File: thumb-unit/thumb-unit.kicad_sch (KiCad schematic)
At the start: 0 parts

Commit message: feat: oyayubi unit
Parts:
- added BT1: Battery, symbol Device:Battery
- added C10: 10uF, symbol Device:C
- added C11, C12: 10nF, symbol Device:C
- added C13, C15, C16: 100nF, symbol Device:C
- added C17: 3.3uF, symbol Device:C
- added D1, D2, D3, D4: D, symbol Device:D
- added J1: Conn_01x10, symbol Connector_Generic:Conn_01x10
- added R2: 10k, symbol Device:R
- added SW1: SW_SPDT, symbol Switch:SW_SPDT
- added SW2, SW3, SW4, SW5: SW_Push, symbol Switch:SW_Push
- added U1: xiao-ble, symbol mcu:xiao-ble
- added U2: PMW3610, sensor:PMW3610, symbol sensor:PMW3610
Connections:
- new net: D3.1 (K), SW4.1
- new net: D4.1 (K), SW5.1
- new net: D2.1 (K), SW3.1
- new net: C13.1, U2.13 (C-)
- new net: C13.2, U2.12 (C+)
- new net: BT1.1 (+), SW1.2 (B)
- new net: D1.1 (K), SW2.1
- new net: C10.1, C11.1, U2.9 (VCP)
- new net +3V3: C12.1, C12.2, C15.2, C16.2, C17.2, J1.1 (Pin_1), R2.1, U1.12 (3V3), U2.1 (+VCSEL), U2.14 (VDD), U2.15 (XYLASER), U2.16 (-VCSEL), U2.6 (VDDIO), U2.7 (~{RESET})
- new net BAT_SW: SW1.1 (A), U1.19 (BAT)
- new net COL0: J1.6 (Pin_6), SW2.2, U1.8 (B9_RX/1.12)
- new net COL1: J1.7 (Pin_7), SW3.2, U1.9 (A7_SCK/1.13)
- new net COL2: J1.8 (Pin_8), SW4.2, U1.10 (A5_MISO/1.14)
- new net COL3: J1.9 (Pin_9), SW5.2, U1.11 (A6_MOSI/1.15)
- new net COL4: J1.10 (Pin_10), U1.22 (NFC2/0.10_H)
- new net GND: BT1.2 (-), C10.2, C11.2, C15.1, C16.1, C17.1, J1.2 (Pin_2), U1.13 (GND), U1.18 (GND), U1.20 (GND), U2.11 (GND)
- new net MOTION: R2.2, U1.3 (A10/0.28), U2.8 (MOTION)
- new net NCS: U1.21 (NFC1/0.09_H), U2.5 (~{CS})
- new net ROW0: J1.3 (Pin_3), U1.4 (A11/0.29)
- new net ROW1: J1.4 (Pin_4), U1.5 (A8_SDA/0.04_H)
- new net ROW2: J1.5 (Pin_5), U1.6 (A9_SCL/0.05_H)
- new net ROW3: D1.2 (A), D2.2 (A), D3.2 (A), D4.2 (A), U1.7 (B8_TX/1.11)
- new net SCLK: U1.2 (A4/0.03_H), U2.3 (SCLK)
- new net SDIO: U1.1 (A2/0.02_H), U2.2 (SDIO)
- no-connect marks 0 -> 6

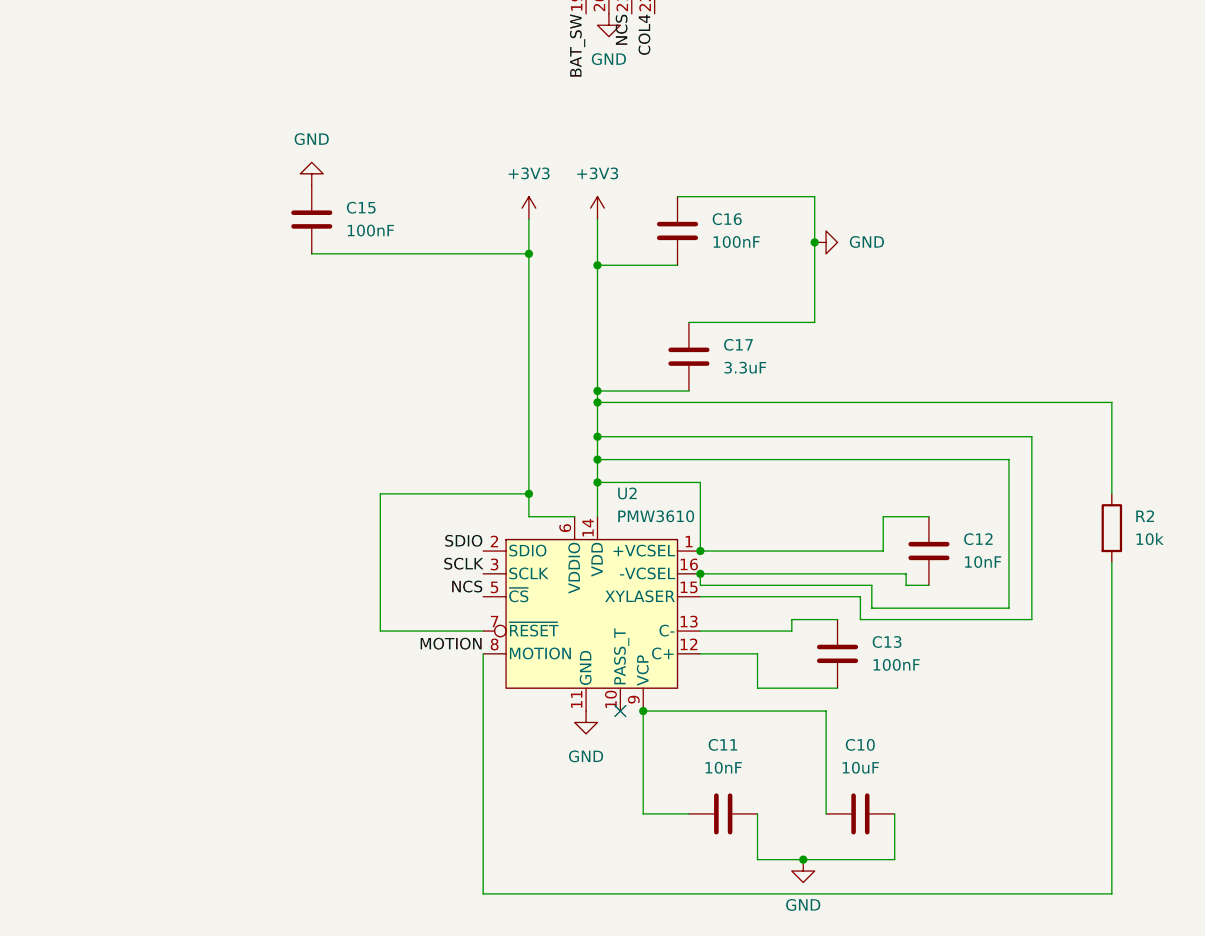
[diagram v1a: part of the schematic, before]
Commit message: feat: add ldo
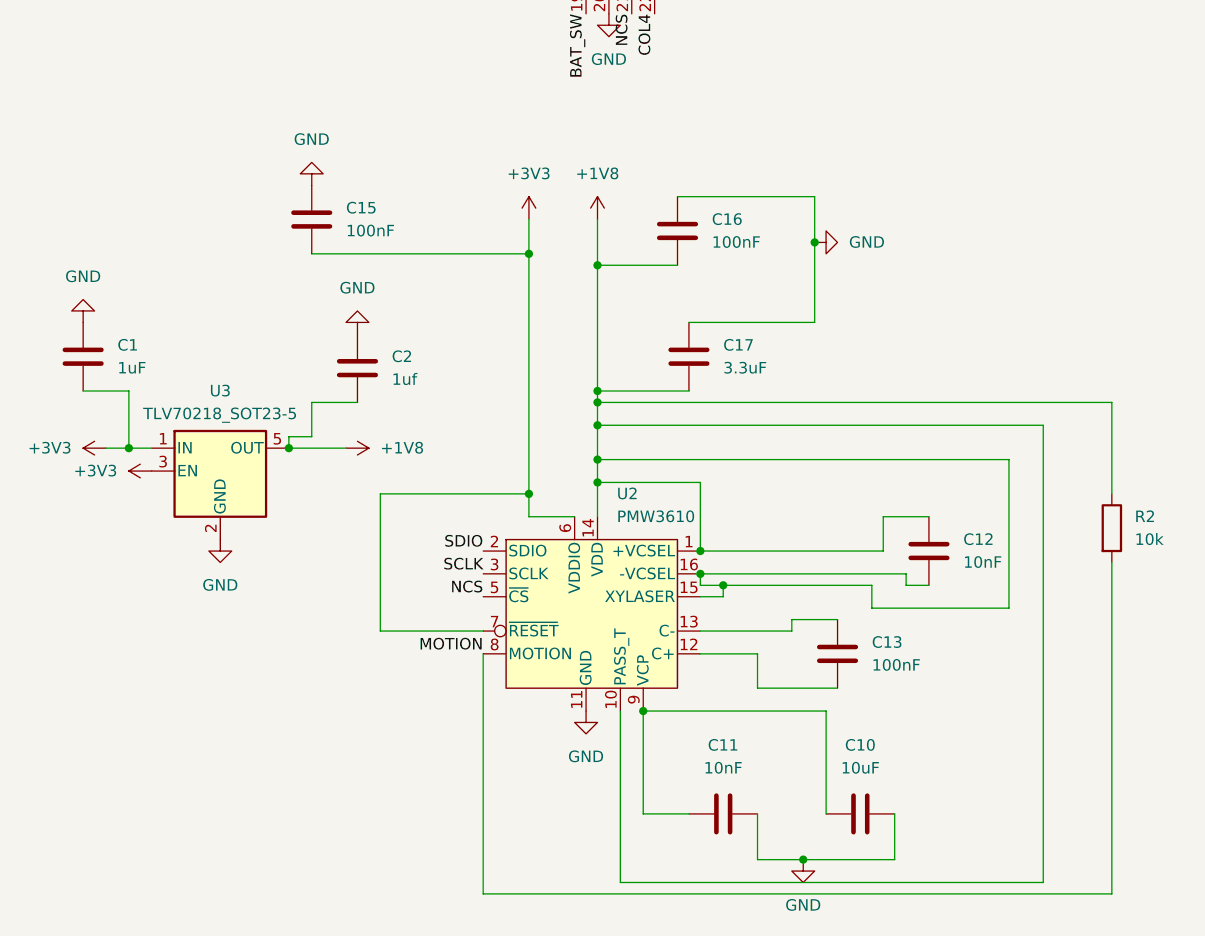
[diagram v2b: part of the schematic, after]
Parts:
- added C1: 1uF, symbol Device:C
- added C2: 1uf, symbol Device:C
- added U3: TLV70218_SOT23-5, Package_TO_SOT_SMD:SOT-23-5, symbol Regulator_Linear:TLV70218_SOT23-5
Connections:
- net +3V3: now also C1.2, U3.1 (IN), U3.3 (EN); no longer C12.1, C12.2, C16.2, C17.2, R2.1, U2.1 (+VCSEL), U2.14 (VDD), U2.15 (XYLASER), U2.16 (-VCSEL)
- net GND: now also C1.1, C2.1, U3.2 (GND)
- net +1V8: now reaches U2.10 (PASS_T)
- net +1V8: now also C12.1, C12.2, C16.2, C17.2, R2.1, U2.1 (+VCSEL), U2.14 (VDD), U2.15 (XYLASER), U2.16 (-VCSEL), C2.2, U3.5 (OUT)
- no-connect marks 6 -> 5

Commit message: feat: フットプリント割り当て
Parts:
- BT1: footprint (none) -> Connector_JST:JST_PH_S2B-PH-K_1x02_P2.00mm_Horizontal
- C1, C11, C12, C13, C15, C16, C17, C2: footprint (none) -> Capacitor_SMD:C_0402_1005Metric
- C10: footprint (none) -> Capacitor_SMD:C_0603_1608Metric
- D1, D2, D3, D4: footprint (none) -> Diode_SMD:D_SOD-123
- J1: footprint (none) -> Connector_FFC-FPC:Hirose_FH12-10S-0.5SH_1x10-1MP_P0.50mm_Horizontal
- R2: footprint (none) -> Resistor_SMD:R_0402_1005Metric
- SW1: footprint (none) -> custom:TGSW_MSK-12D19
- SW2, SW3, SW4, SW5: footprint (none) -> PCM_Switch_Keyboard_Hotswap_Kailh:SW_Hotswap_Kailh_Choc_V1V2_1.00u
- U1: footprint (none) -> mcu:xiao-ble-smd
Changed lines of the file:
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@@
 			)
 		)
-		(property "Footprint" ""
+		(property "Footprint" "Diode_SMD:D_SOD-123"
 			(at 190.5 114.3 0)
 			(effects
@@
 			)
 		)
-		(property "Footprint" ""
+		(property "Footprint" "Resistor_SMD:R_0402_1005Metric"
 			(at 131.572 149.86 90)
 			(effects
@@
 			)
 		)
-		(property "Footprint" ""
+		(property "Footprint" "Diode_SMD:D_SOD-123"
 			(at 204.47 114.3 0)
 			(effects
@@
 			)
 		)
-		(property "Footprint" ""
+		(property "Footprint" "Connector_FFC-FPC:Hirose_FH12-10S-0.5SH_1x10-1MP_P0.50mm_Horizontal"
 			(at 246.38 125.73 0)
 			(effects
@@
 			)
 		)
-		(property "Footprint" ""
+		(property "Footprint" "Diode_SMD:D_SOD-123"
 			(at 176.53 114.3 0)
 			(effects
@@
 			)
 		)
-		(property "Footprint" ""
+		(property "Footprint" "Capacitor_SMD:C_0402_1005Metric"
 			(at 103.8352 167.64 0)
 			(effects
@@
 			)
 		)
-		(property "Footprint" ""
+		(property "Footprint" "Capacitor_SMD:C_0402_1005Metric"
 			(at 20.0152 134.62 0)
 			(effects
@@
 			)
 		)
-		(property "Footprint" ""
+		(property "Footprint" "Connector_JST:JST_PH_S2B-PH-K_1x02_P2.00mm_Horizontal"
 			(at 161.29 157.226 90)
 			(effects
@@
 			)
 		)
-		(property "Footprint" ""
+		(property "Footprint" "Capacitor_SMD:C_0402_1005Metric"
 			(at 50.4952 135.89 0)
 			(effects
@@
 			)
 		)
-		(property "Footprint" ""
+		(property "Footprint" "mcu:xiao-ble-smd"
 			(at 73.66 71.12 0)
 			(effects
@@
 			)
 		)
-		(property "Footprint" ""
+		(property "Footprint" "PCM_Switch_Keyboard_Hotswap_Kailh:SW_Hotswap_Kailh_Choc_V1V2_1.00u"
 			(at 176.53 124.46 0)
 			(effects
@@
 			)
 		)
-		(property "Footprint" ""
+		(property "Footprint" "Capacitor_SMD:C_0402_1005Metric"
 			(at 113.9952 156.21 0)
 			(effects
@@
 			)
 		)
-		(property "Footprint" ""
+		(property "Footprint" "Capacitor_SMD:C_0402_1005Metric"
 			(at 86.0552 120.65 0)
 			(effects
@@
 			)
 		)
-		(property "Footprint" ""
+		(property "Footprint" "Diode_SMD:D_SOD-123"
 			(at 162.56 114.3 0)
 			(effects
@@
 			)
 		)
-		(property "Footprint" ""
+		(property "Footprint" "Capacitor_SMD:C_0402_1005Metric"
 			(at 87.3252 134.62 0)
 			(effects
@@
 			)
 		)
-		(property "Footprint" ""
+		(property "Footprint" "PCM_Switch_Keyboard_Hotswap_Kailh:SW_Hotswap_Kailh_Choc_V1V2_1.00u"
 			(at 204.47 124.46 0)
 			(effects
@@
 			)
 		)
-		(property "Footprint" ""
+		(property "Footprint" "Capacitor_SMD:C_0402_1005Metric"
 			(at 45.4152 119.38 0)
 			(effects
@@
 			)
 		)
-		(property "Footprint" ""
+		(property "Footprint" "Capacitor_SMD:C_0402_1005Metric"
 			(at 93.98 180.6448 0)
 			(effects
@@
 			)
 		)
-		(property "Footprint" ""
+		(property "Footprint" "Capacitor_SMD:C_0603_1608Metric"
 			(at 109.22 180.6448 0)
 			(effects
@@
 			)
 		)
-		(property "Footprint" ""
+		(property "Footprint" "PCM_Switch_Keyboard_Hotswap_Kailh:SW_Hotswap_Kailh_Choc_V1V2_1.00u"
 			(at 162.56 124.46 0)
 			(effects
@@
 			)
 		)
-		(property "Footprint" ""
+		(property "Footprint" "custom:TGSW_MSK-12D19"
 			(at 184.15 158.75 0)
 			(effects
@@
 			)
 		)
-		(property "Footprint" ""
+		(property "Footprint" "PCM_Switch_Keyboard_Hotswap_Kailh:SW_Hotswap_Kailh_Choc_V1V2_1.00u"
 			(at 190.5 124.46 0)
 			(effects

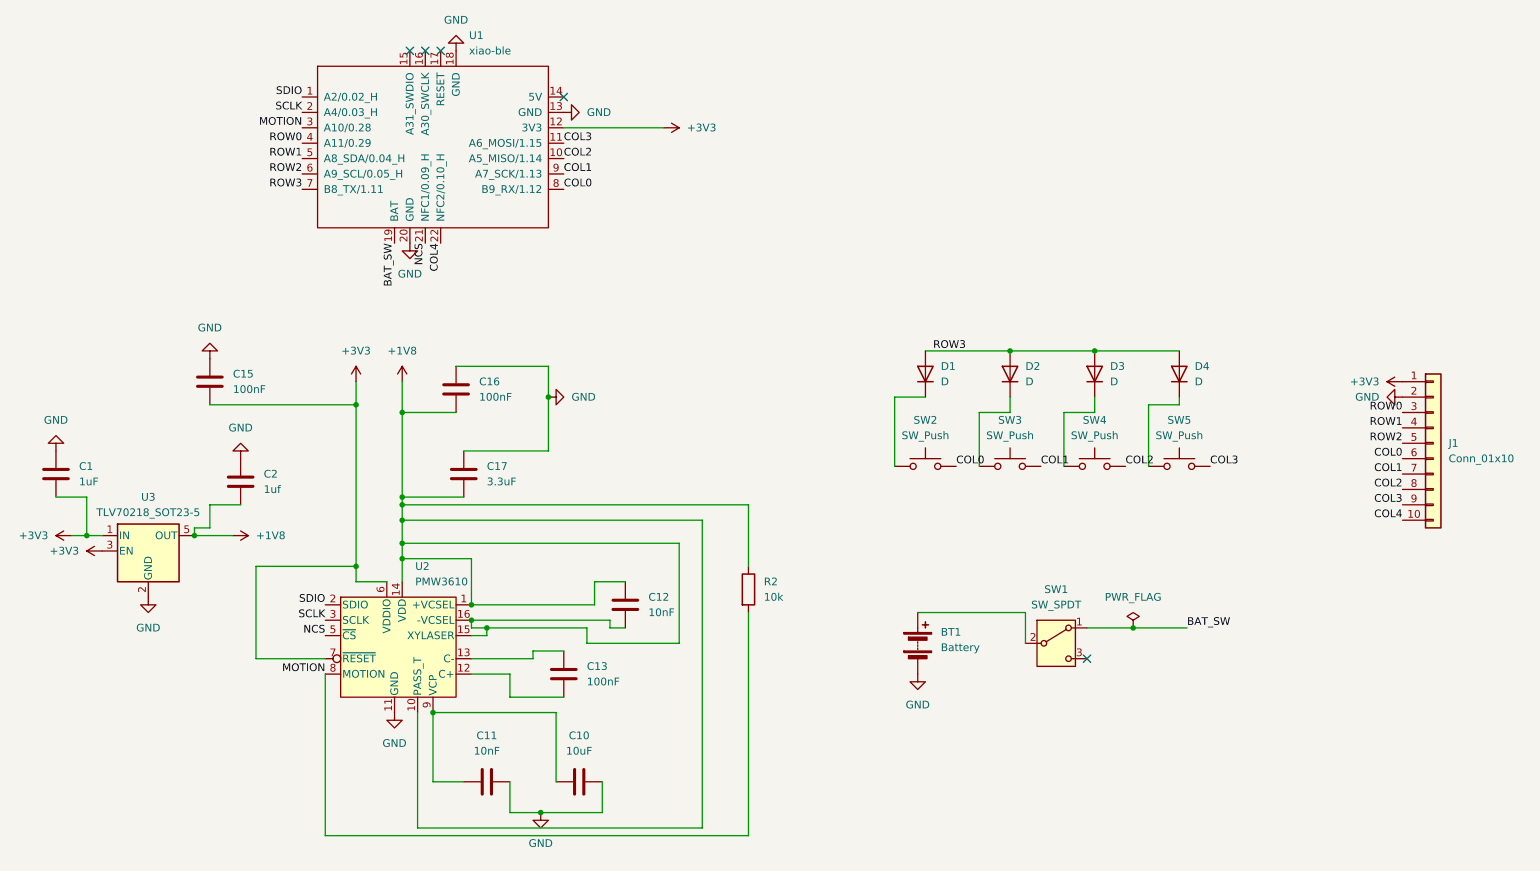
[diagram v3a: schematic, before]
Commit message: fix: 親指ユニットの回路図
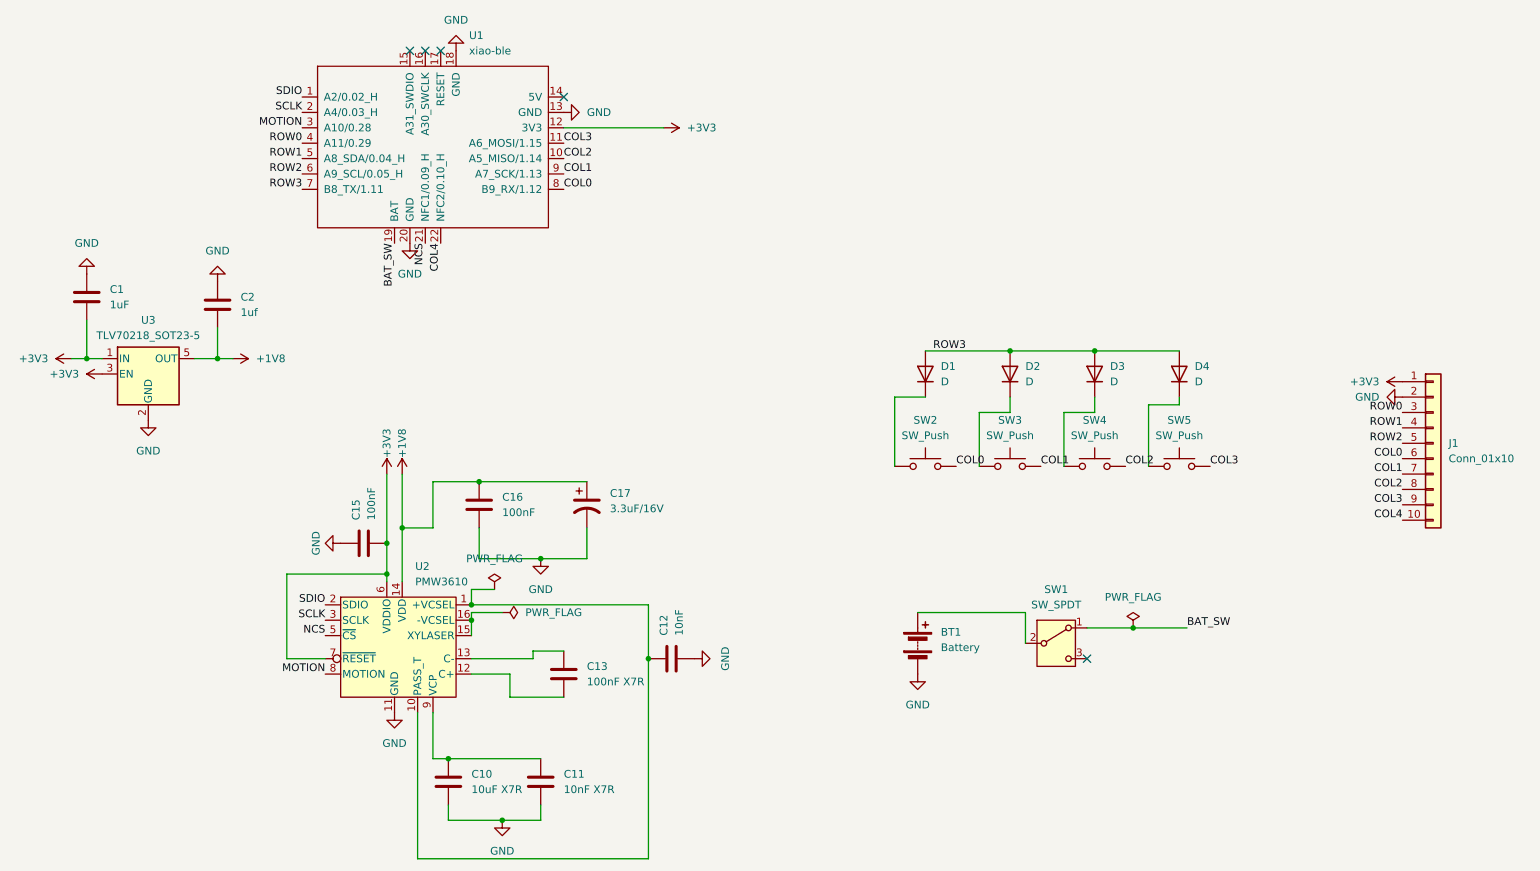
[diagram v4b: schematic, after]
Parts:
- removed C17: 3.3uF, Capacitor_SMD:C_0402_1005Metric, symbol Device:C
- removed R2: 10k, Resistor_SMD:R_0402_1005Metric, symbol Device:R
- added C17: 3.3uF/16V, symbol Device:C_Polarized_US
- BT1: footprint Connector_JST:JST_PH_S2B-PH-K_1x02_P2.00mm_Horizontal -> Connector_Molex:Molex_PicoBlade_53048-0210_1x02_P1.25mm_Horizontal
- C10: value 10uF -> 10uF X7R
- C11: value 10nF -> 10nF X7R
- C13: value 100nF -> 100nF X7R
- SW2, SW3, SW4, SW5: footprint PCM_Switch_Keyboard_Hotswap_Kailh:SW_Hotswap_Kailh_Choc_V1V2_1.00u -> PCM_Switch_Keyboard_Hotswap_Kailh:SW_Hotswap_Kailh_Choc_V2_1.00u
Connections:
- net +1V8: now also C16.1, C17.1; no longer C12.1, C12.2, C16.2, U2.1 (+VCSEL), U2.10 (PASS_T), U2.15 (XYLASER), U2.16 (-VCSEL)
- net GND: now also C10.1, C11.1, C12.2, C16.2, C17.2; no longer C10.2, C11.2, C16.1
- new net: C12.1, U2.1 (+VCSEL), U2.10 (PASS_T)
- new net: C10.2, C11.2, U2.9 (VCP)
- new net: U2.15 (XYLASER), U2.16 (-VCSEL)
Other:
- moved on the sheet: C1, C10, C11, C12, C15, C16, C2, U3

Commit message: feat: 親指ユニットのpcb設計
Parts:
- C17: footprint (none) -> Capacitor_SMD:C_0603_1608Metric
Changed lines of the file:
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@@
 			)
 		)
-		(property "Footprint" ""
+		(property "Footprint" "Capacitor_SMD:C_0603_1608Metric"
 			(at 106.68 135.89 0)
 			(effects

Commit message: feat: 回路図完成
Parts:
- added R1: 10k, Resistor_SMD:R_0603_1608Metric, symbol Device:R
- BT1: footprint Connector_Molex:Molex_PicoBlade_53048-0210_1x02_P1.25mm_Horizontal -> Connector_Molex:Molex_PicoBlade_53261-0271_1x02-1MP_P1.25mm_Horizontal
- U1: footprint mcu:xiao-ble-smd -> mcu:xiao-ble-tht
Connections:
- net +3V3: now also R1.1; no longer U2.7 (~{RESET})
- new net: R1.2, U2.7 (~{RESET})
